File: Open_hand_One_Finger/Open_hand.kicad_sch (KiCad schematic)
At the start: 17 parts, among them J1 Conn_ARM_JTAG_SWD_10, J2 DF37C-24DP-0.4V(51), U2 MAX32660GTP, Y1 32.768kHz,6pF

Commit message: new copper pour rules
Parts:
- J2: footprint (none) -> DF37C-24DP-0.4V(51):DF37C-24DP-0.4V(51)
- R1: footprint (none) -> Resistor_SMD:R_0603_1608Metric
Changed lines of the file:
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@@
       (effects (font (size 1.27 1.27)))
     )
-    (property "Footprint" "" (at 255.27 82.55 0)
+    (property "Footprint" "DF37C-24DP-0.4V(51):DF37C-24DP-0.4V(51)" (at 255.27 82.55 0)
       (effects (font (size 1.27 1.27)) hide)
     )
@@
       (effects (font (size 1.27 1.27)) (justify left))
     )
-    (property "Footprint" "" (at 78.486 139.954 90)
-      (effects (font (size 1.27 1.27)) hide)
+    (property "Footprint" "Resistor_SMD:R_0603_1608Metric" (at 78.486 139.954 90)
+      (effects (font (size 1.27 1.27)))
     )
     (property "Datasheet" "~" (at 77.47 139.7 0)

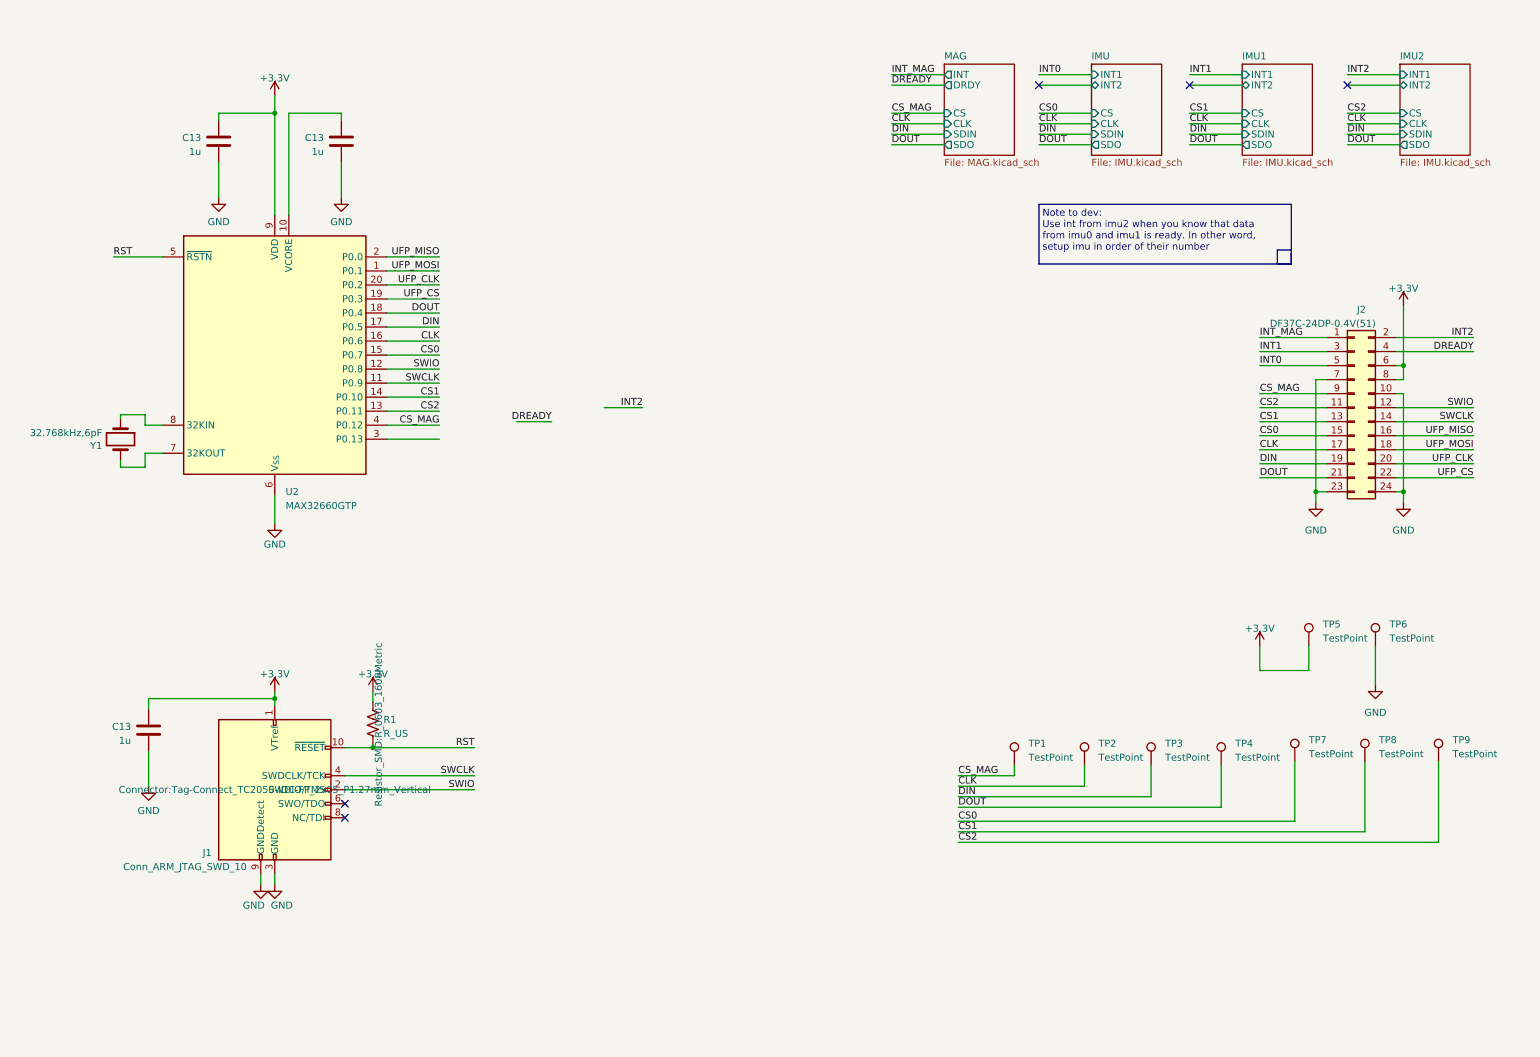
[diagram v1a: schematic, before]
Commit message: ajout des infos dans la cartouche
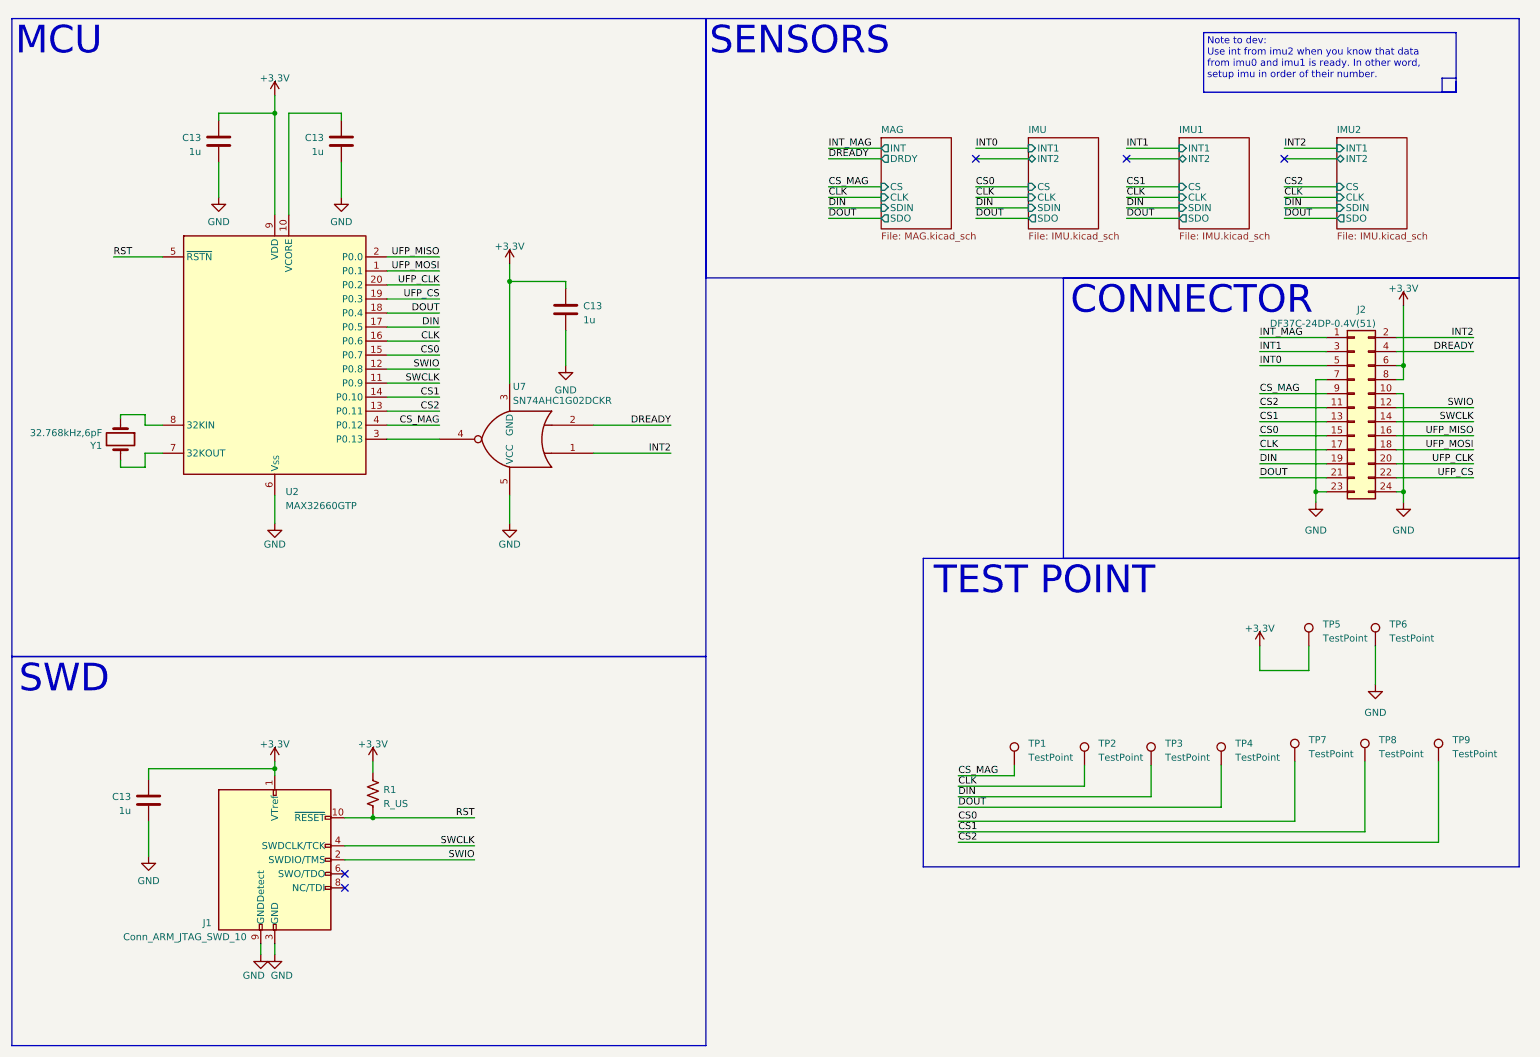
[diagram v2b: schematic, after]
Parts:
- added C13: 1u, Capacitor_SMD:C_0603_1608Metric, symbol Device:C
- added U7: SN74AHC1G02DCKR, Package_TO_SOT_SMD:SOT-353_SC-70-5, symbol 74xGxx:74AHC1G02
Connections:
- net +3.3V: now also C13.1, U7.3 (GND)
- net DREADY: now also U7.2
- net GND: now also C13.2, U7.5 (VCC)
- net INT2: now also U7.1
- net at U2.3 (P0.13): now also U7.4
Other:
- note added: "CONNECTOR"
- note added: "MCU"
- note added: "Note to dev: Use int from imu2 when you know that data from imu0 and imu1 is ready. In other word, setup imu in order of their number."
- note added: "SENSORS"
- note added: "SWD"
- note added: "TEST POINT"
- note removed: "Note to dev: Use int from imu2 when you know that data from imu0 and imu1 is ready. In other word, setup imu in order of their number"
- title: (none) -> Open hand project main schematic page
- moved on the sheet: C13, J1, R1
